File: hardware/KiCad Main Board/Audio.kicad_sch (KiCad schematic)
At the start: 41 parts, among them J6 SPK_CONN_INT, J7 SPK_2.5MM SJ1-2503A, J8 MIC_3.5MM PJ-307C, Q7 AO3401A, U12 TLV320AIC3100, U13 AMS1117-1.8, U8 SPH0645LM4H

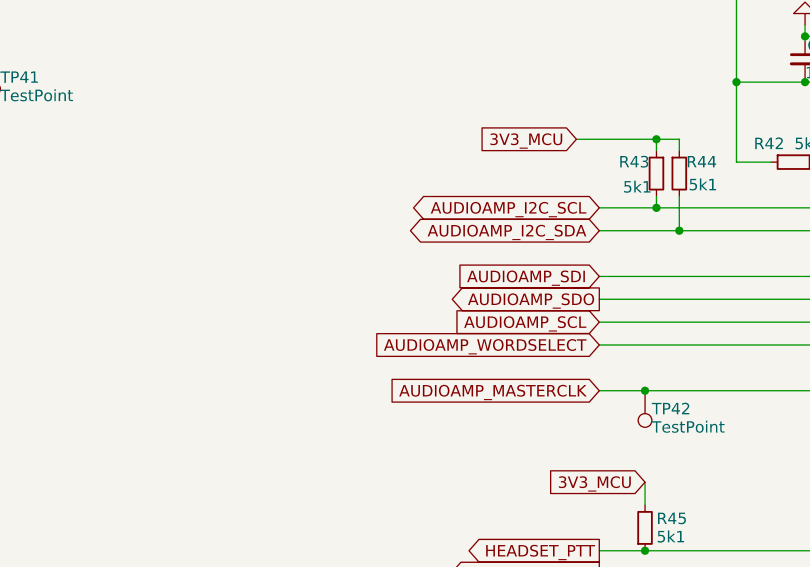
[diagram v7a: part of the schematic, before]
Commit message: more design on the RF module
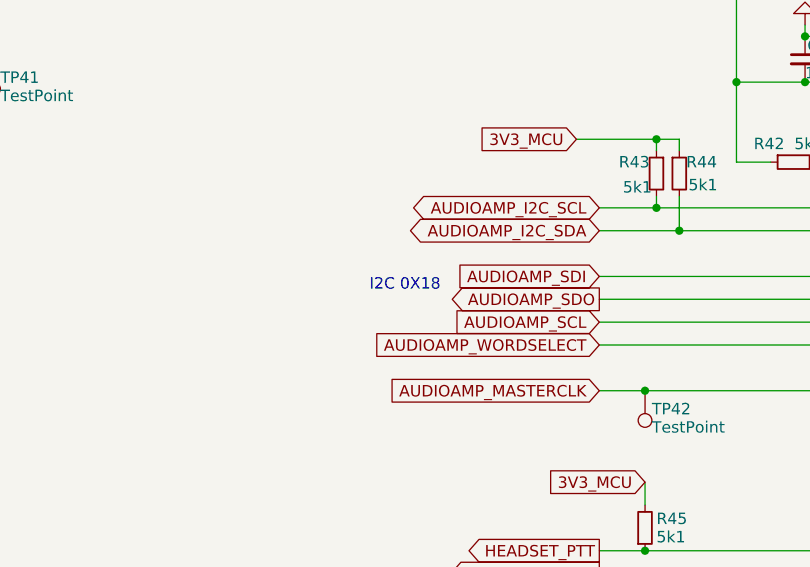
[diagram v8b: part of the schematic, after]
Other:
- note added: "I2C 0X18"
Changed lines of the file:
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@@
+		)
+	)
+	(text "I2C 0X18"
+		(exclude_from_sim no)
+		(at 116.84 103.886 0)
+		(effects
+			(font
+				(size 1.27 1.27)
+			)
 		)
 	)
